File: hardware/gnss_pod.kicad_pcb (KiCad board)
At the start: 2 copper layers, 89.1 x 92.1 mm, 20 parts, among them IC1 CDNBS08-PLC03-6, J1 SQT-110-01-L-D, J2 SSQ-126-04-G-D, J3 SSQ-126-04-G-D, J5 Conn_01x02_Pin, U1 TCAN334G

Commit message: Added some connections, infos and USB footprint
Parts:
- added FB1: BMC-Q1EY0080M, Inductor_SMD:L_0402_1005Metric_Pad0.77x0.64mm_HandSolder, F.Cu at (121.2, 87.4)
- added FB2: BMC-Q1EY0080M, Inductor_SMD:L_0402_1005Metric_Pad0.77x0.64mm_HandSolder, F.Cu at (124.0, 92.6)
- added G***: LOGO, LOGO, F.Cu at (150.0, 92.0)
- added G***: LOGO, lib:spacelab-logo, F.Cu at (184.2, 131.6)
- added G***: LOGO, lib:spacelab-logo, B.Cu at (184.2, 131.6)
- added J4: Conn_01x02_Pin, footprints:532614002, F.Cu at (108.0, 106.2)
- added J6: USB_C_Receptacle_USB2.0_16P, footprints:USB4110GFA, F.Cu at (190.5, 81.9)
- moved R2 7.45 mm to (113.8, 92.4)
- moved IC1 2.70 mm to (119.1, 92.5)
- moved C2 1.88 mm to (122.7, 88.8), turned to 0 degrees
- moved R1 1.35 mm to (117.8, 73.7), turned to 180 degrees
- moved C3 1.19 mm to (124.8, 94.5)
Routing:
- net /TX2: track 0.00 -> 65.4 mm, vias 0 -> 2
- net /RX2: track 0.00 -> 60.8 mm
- net /USB_N: track 0.00 -> 44.0 mm, vias 0 -> 2
- net /USB_P: track 0.00 -> 43.8 mm, vias 0 -> 2
- net /CAN2RX: track 0.00 -> 39.0 mm, vias 0 -> 2
- net Net-(U1-CANL): track 0.00 -> 38.2 mm, vias 0 -> 2
- net /CAN2TX: track 0.00 -> 26.4 mm
- net VCC: track 28.3 -> 52.4 mm
- net Net-(U1-CANH): track 0.00 -> 23.1 mm
- net /CAN-: track 0.00 -> 15.5 mm
- net /CAN+: track 0.00 -> 13.2 mm
- net /TX1: track 32.0 -> 35.2 mm
- net Net-(U1-TXD): track 0.00 -> 1.75 mm
- net /RX1: track 20.2 -> 20.8 mm
- net GNDREF: track 0.45 -> 0.42 mm, vias 1 -> 19
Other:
- outline, holes or cut-outs redrawn
- board text added: "GNSS"
- board text added: "HOLDER"
- board text added: "OEM719 RECEIVER"
- board text added: "v1.0"
- board text removed: "OEM719 NOMINAL"

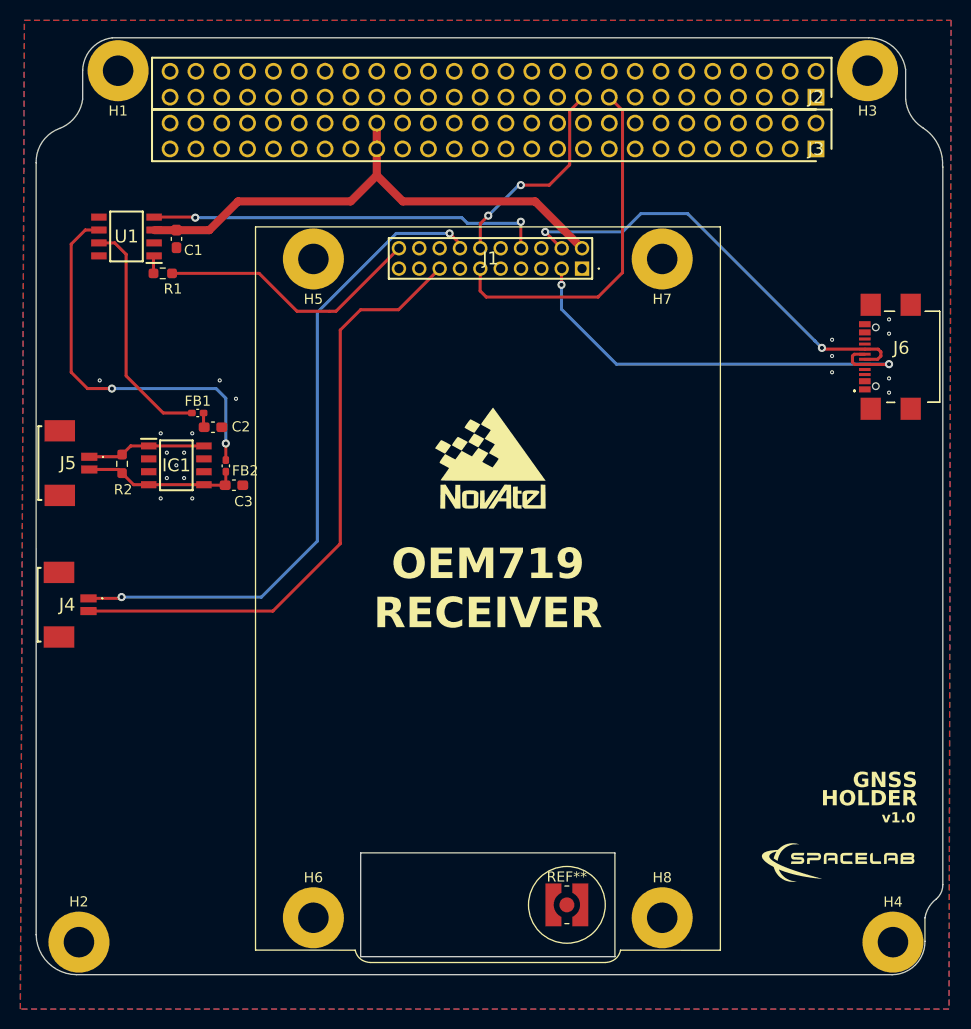
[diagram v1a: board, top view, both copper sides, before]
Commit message: Receiver Flipped, Added Simple Match lenght traces, Added more silkscreen comments
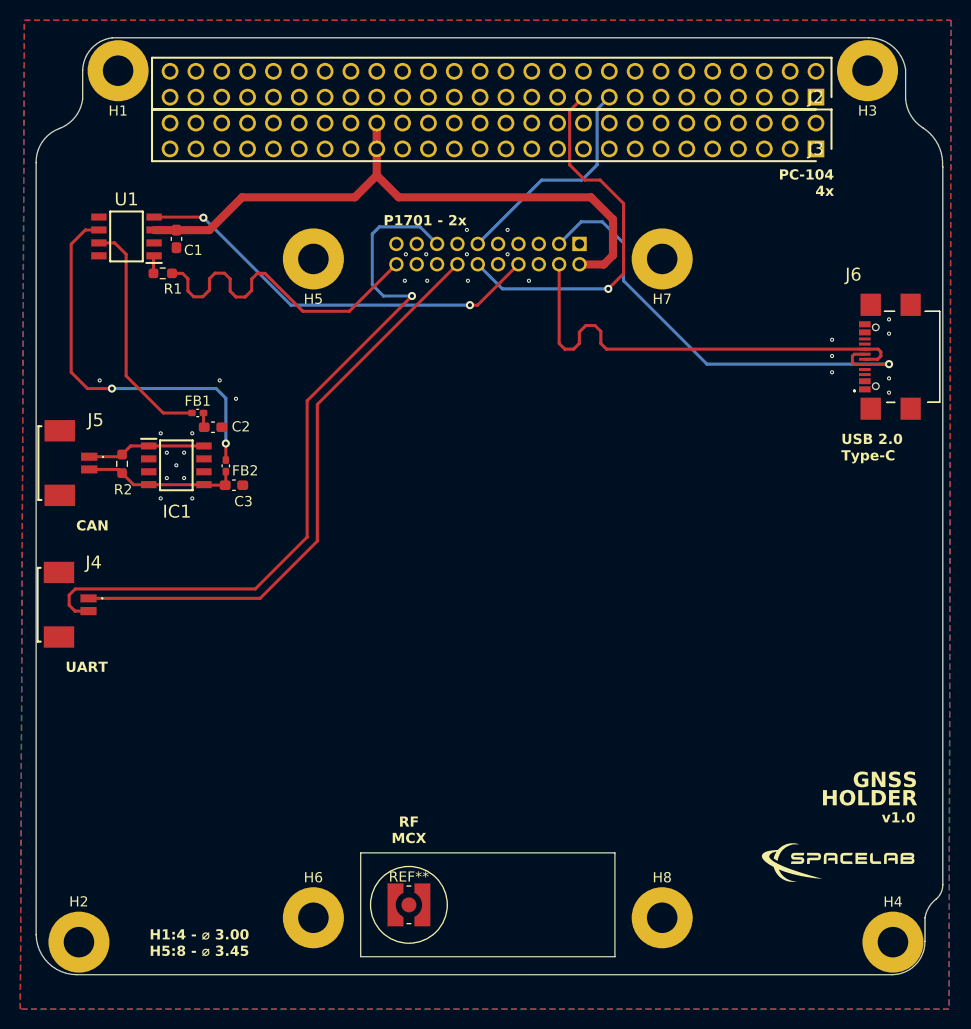
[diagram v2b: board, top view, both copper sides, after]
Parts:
- G***, J1: moved to B.Cu
- moved REF** 15.5 mm to (142.0, 135.8)
- moved J1 2.44 mm to (158.8, 70.8)
- turned G*** to 180 degrees
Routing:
- net /RX1: track 20.8 -> 36.9 mm, vias 2 -> 1
- net /TX1: track 35.2 -> 22.1 mm
- net /RX2: track 60.8 -> 73.6 mm, vias 0 -> 1
- net VCC: track 52.4 -> 61.5 mm
- net /TX2: track 65.4 -> 57.8 mm, vias 2 -> 0
- net /CAN2TX: track 26.4 -> 32.1 mm
- net /USB_N: track 44.0 -> 46.9 mm, vias 2 -> 1
- net /CAN2RX: track 39.0 -> 41.1 mm
- net /USB_P: track 43.8 -> 45.2 mm, vias 2 -> 0
- net GNDREF: vias 19 -> 29
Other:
- board text added: "CAN"
- board text added: "H1:4 - ⌀ 3.00 H5:8 - ⌀ 3.45"
- board text added: "P1701 - 2x"
- board text added: "PC-104 4x"
- board text added: "RF MCX"
- board text added: "UART"
- board text added: "USB 2.0 Type-C"
- board text removed: "2x"

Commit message: Trace match, PC104 adjusted, Hole Diameter.
- PC104 was mirrored;
- USB Trace is match by less then 1mm;
- CAN is not trace matched;
- Adjusted hole diameter for OEM719 Receiver (3mm -> 3.45mm);
- Trace is bigger for VCC.
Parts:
- added FB3: FerriteBead_Small, Inductor_SMD:L_0603_1608Metric, F.Cu at (187.4, 90.6)
- added R3: 5K1, Resistor_SMD:R_0603_1608Metric, F.Cu at (183.8, 84.0)
- added R4: 5K1, Resistor_SMD:R_0603_1608Metric, F.Cu at (183.8, 79.3)
- J2: renamed from J3; moved to B.Cu
- J3: renamed from J2; moved to B.Cu
- moved J2 63.8 mm to (118.3, 61.4), turned to 180 degrees
- moved J3 63.8 mm to (118.3, 56.4), turned to 180 degrees
- moved C2 1.85 mm to (120.9, 88.8), turned to 180 degrees
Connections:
- J2 pad 17: unconnected-(J3-Pad17) -> /TX1
- J2 pad 19: unconnected-(J3-Pad19) -> /RX1
- J2 pad 35: VCC -> unconnected-(J2-Pad35)
- J2 pad 36: VCC -> unconnected-(J2-Pad36)
- J3 pad 17: /TX1 -> unconnected-(J3-Pad17)
- J3 pad 19: /RX1 -> unconnected-(J3-Pad19)
- J3 pad 35: unconnected-(J2-Pad35) -> VCC
- J3 pad 36: unconnected-(J2-Pad36) -> VCC
- J6 pad A5: unconnected-(J6-CC1-PadA5) -> Net-(J6-CC1)
- J6 pad B5: unconnected-(J6-CC2-PadB5) -> Net-(J6-CC2)
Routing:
- net /RX1: track 36.9 -> 27.1 mm
- net Net-(U1-CANL): track 38.2 -> 29.0 mm, vias 2 -> 0
- net /USB_P: track 45.2 -> 54.1 mm
- net /TX1: track 22.1 -> 15.3 mm
- net VCC: track 61.5 -> 68.1 mm
- net /CAN2TX: track 32.1 -> 25.5 mm
- net Net-(J6-CC1): track 0.00 -> 3.09 mm
- net Net-(J6-CC2): track 0.00 -> 3.02 mm
- net /CAN+: track 13.2 -> 15.2 mm
- net Net-(U1-TXD): track 1.75 -> 0.09 mm
- net Net-(U1-CANH): track 23.1 -> 21.4 mm
- net unconnected-(J3-Pad40): track 0.70 -> 0.00 mm
- net unconnected-(J3-Pad14): track 0.00 -> 0.70 mm
- net /RX2: track 73.6 -> 74.2 mm
- net /USB_N: track 46.9 -> 47.5 mm
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- added copper zone on F.Cu, net Net-(J6-SHIELD)
- added copper zone on F.Cu, net Net-(U1-TXD)
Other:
- board text added: "1"
- board text added: "20"
- board text added: "MPX (1-4)"
- board text added: "P1701"
- board text added: "Verify if PCBWay can cut this hole of 3.45 diameter"
- board text added: "Verify position of the PC104 on the board"
- board text added: "{dblquote}Space?! SPACE! SPAAAAACE!!!{dblquote} - SC"
- board text removed: "P1701 - 2x"
